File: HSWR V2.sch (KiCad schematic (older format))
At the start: 24 parts, among them P1 USB_B, P2 Interface, P3 IN+, P4 IN-, P5 MOTOR3, P6 MOTOR2, P7 MOTOR1

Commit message: - 100A in 50A geändert
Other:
- note added: "HSWR V2.0 200V 50A"
- note removed: "HSWR V2.0 200V 100A"
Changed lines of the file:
@@
 encoding utf-8
 Sheet 1 7
-Title "HSWR V2.0 200V 100A"
+Title "HSWR V2.0 200V 50A"
 Date "2017-02-05"
 Rev "2.0"
@@
 $EndComp
 Text Notes 800  1200 0    340  ~ 68
-HSWR V2.0 200V 100A
+HSWR V2.0 200V 50A
 $Bitmap
 Pos 10350 3100
@@
 C8 C8 08 D2 A9 87 39 1B F9 3D 64 10 3C A5 22 3B 19 76 2F 98 2B 2B 2B 1E 8F A7 AB AB 0B FB AC 1D
 B9 73 C8 EF 2C EC 8D 33 57 03 96 70 05 29 43 0C 6A C5 A8 D7 30 9E 87 2D DE BE E8 EA 73 2F 9C 18
-F1 B3 C3 9F 6D FA 1E FF 03 71 17 46 7E 55 DF FF 4E 00 00 00 00 49 45 4E 44 AE 42 60 82 0E
+F1 B3 C3 9F 6D FA 1E FF 03 71 17 46 7E 55 DF FF 4E 00 00 00 00 49 45 4E 44 AE 42 60 82 AB
 EndData
 $EndBitmap
@@
 20 08 82 20 08 12 3C 28 79 08 82 20 08 82 20 2D 08 4A 1E 82 20 08 82 20 48 0B 82 92 87 20 08 82
 20 08 D2 82 A0 E4 21 08 82 20 08 82 B4 20 28 79 08 82 20 08 82 20 2D 08 4A 1E 82 20 08 82 20 48
-0B F2 FF 19 12 7F 86 40 CA 02 9D 00 00 00 00 49 45 4E 44 AE 42 60 82 F3
+0B F2 FF 19 12 7F 86 40 CA 02 9D 00 00 00 00 49 45 4E 44 AE 42 60 82 FF
 EndData
 $EndBitmap
@@
 20 08 82 84 0E 7A 08 41 10 04 29 27 E8 21 04 41 10 A4 9C A0 87 10 04 41 90 72 82 1E 42 10 04 41
 CA 09 7A 08 41 10 04 29 27 E8 21 04 41 10 A4 9C FC 1F 60 28 4A EE 61 E4 B4 21 00 00 00 00 49 45
-4E 44 AE 42 60 82 00
+4E 44 AE 42 60 82 7F
 EndData
 $EndBitmap

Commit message: ~ removed/optionalised INA240 input filter ~ raised load resisitance of sense resistors for lower power loss ~ adopted old division factor on phase voltage sense deviders
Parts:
- R7: value 64k9 -> 160k
- R8: value 1k -> 3k3
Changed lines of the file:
@@
 C8 C8 08 D2 A9 87 39 1B F9 3D 64 10 3C A5 22 3B 19 76 2F 98 2B 2B 2B 1E 8F A7 AB AB 0B FB AC 1D
 B9 73 C8 EF 2C EC 8D 33 57 03 96 70 05 29 43 0C 6A C5 A8 D7 30 9E 87 2D DE BE E8 EA 73 2F 9C 18
-F1 B3 C3 9F 6D FA 1E FF 03 71 17 46 7E 55 DF FF 4E 00 00 00 00 49 45 4E 44 AE 42 60 82 AB
+F1 B3 C3 9F 6D FA 1E FF 03 71 17 46 7E 55 DF FF 4E 00 00 00 00 49 45 4E 44 AE 42 60 82 F5
 EndData
 $EndBitmap
@@
 20 08 82 20 08 12 3C 28 79 08 82 20 08 82 20 2D 08 4A 1E 82 20 08 82 20 48 0B 82 92 87 20 08 82
 20 08 D2 82 A0 E4 21 08 82 20 08 82 B4 20 28 79 08 82 20 08 82 20 2D 08 4A 1E 82 20 08 82 20 48
-0B F2 FF 19 12 7F 86 40 CA 02 9D 00 00 00 00 49 45 4E 44 AE 42 60 82 FF
+0B F2 FF 19 12 7F 86 40 CA 02 9D 00 00 00 00 49 45 4E 44 AE 42 60 82 00
 EndData
 $EndBitmap
@@
 P 5200 4350
 F 0 "R7" V 5280 4350 50  0000 C CNN
-F 1 "64k9" V 5200 4350 50  0000 C CNN
+F 1 "160k" V 5200 4350 50  0000 C CNN
 F 2 "Resistors_SMD:R_0805" V 5130 4350 30  0001 C CNN
 F 3 "" H 5200 4350 30  0000 C CNN
@@
 P 5200 4650
 F 0 "R8" V 5280 4650 50  0000 C CNN
-F 1 "1k" V 5200 4650 50  0000 C CNN
+F 1 "3k3" V 5200 4650 50  0000 C CNN
 F 2 "Resistors_SMD:R_0805" V 5130 4650 30  0001 C CNN
 F 3 "" H 5200 4650 30  0000 C CNN

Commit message: - changed dividers to 220k vs 3k3 - changed hall supply to +5V instead of +3V3
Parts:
- P1: symbol USB_B -> USB_B-RESCUE-HSWR_V2
- R7: value 160k -> 220k
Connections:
- wire segments 79 -> 77
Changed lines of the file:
@@
 C8 C8 08 D2 A9 87 39 1B F9 3D 64 10 3C A5 22 3B 19 76 2F 98 2B 2B 2B 1E 8F A7 AB AB 0B FB AC 1D
 B9 73 C8 EF 2C EC 8D 33 57 03 96 70 05 29 43 0C 6A C5 A8 D7 30 9E 87 2D DE BE E8 EA 73 2F 9C 18
-F1 B3 C3 9F 6D FA 1E FF 03 71 17 46 7E 55 DF FF 4E 00 00 00 00 49 45 4E 44 AE 42 60 82 F5
+F1 B3 C3 9F 6D FA 1E FF 03 71 17 46 7E 55 DF FF 4E 00 00 00 00 49 45 4E 44 AE 42 60 82
 EndData
 $EndBitmap
@@
 20 08 82 20 08 12 3C 28 79 08 82 20 08 82 20 2D 08 4A 1E 82 20 08 82 20 48 0B 82 92 87 20 08 82
 20 08 D2 82 A0 E4 21 08 82 20 08 82 B4 20 28 79 08 82 20 08 82 20 2D 08 4A 1E 82 20 08 82 20 48
-0B F2 FF 19 12 7F 86 40 CA 02 9D 00 00 00 00 49 45 4E 44 AE 42 60 82 00
+0B F2 FF 19 12 7F 86 40 CA 02 9D 00 00 00 00 49 45 4E 44 AE 42 60 82
 EndData
 $EndBitmap
@@
 P 5200 4350
 F 0 "R7" V 5280 4350 50  0000 C CNN
-F 1 "160k" V 5200 4350 50  0000 C CNN
+F 1 "220k" V 5200 4350 50  0000 C CNN
 F 2 "Resistors_SMD:R_0805" V 5130 4350 30  0001 C CNN
 F 3 "" H 5200 4350 30  0000 C CNN
@@
 20 08 82 84 0E 7A 08 41 10 04 29 27 E8 21 04 41 10 A4 9C A0 87 10 04 41 90 72 82 1E 42 10 04 41
 CA 09 7A 08 41 10 04 29 27 E8 21 04 41 10 A4 9C FC 1F 60 28 4A EE 61 E4 B4 21 00 00 00 00 49 45
-4E 44 AE 42 60 82 7F
+4E 44 AE 42 60 82
 EndData
 $EndBitmap
 $Comp
-L +3V3 #PWR013
-U 1 1 5899E248
-P 1300 4300
-F 0 "#PWR013" H 1300 4150 50  0001 C CNN
-F 1 "+3V3" V 1300 4550 50  0000 C CNN
-F 2 "" H 1300 4300 60  0000 C CNN
-F 3 "" H 1300 4300 60  0000 C CNN
-	1    1300 4300
-	0    1    1    0
-$EndComp
-$Comp
 L GND-RESCUE-BLDC_4 #PWR014
 U 1 1 5899E249
@@
 $EndComp
 $Comp
-L USB_B P1
+L USB_B-RESCUE-HSWR_V2 P1
 U 1 1 5899E24E
 P 950 3050
@@
 L +12VA #PWR022
 U 1 1 5899E265
-P 1350 3650
-F 0 "#PWR022" H 1350 3500 50  0001 C CNN
-F 1 "+12VA" H 1350 3790 50  0000 C CNN
-F 2 "" H 1350 3650 60  0000 C CNN
-F 3 "" H 1350 3650 60  0000 C CNN
-	1    1350 3650
-	1    0    0    -1
+P 1300 3700
+F 0 "#PWR022" H 1300 3550 50  0001 C CNN
+F 1 "+12VA" V 1300 3950 50  0000 C CNN
+F 2 "" H 1300 3700 60  0000 C CNN
+F 3 "" H 1300 3700 60  0000 C CNN
+	1    1300 3700
+	0    1    1    0
 $EndComp
-Wire Wire Line
-	1350 3650 1350 3700
-Wire Wire Line
-	1350 3700 1300 3700
 NoConn ~ 2550 4000
 $Comp
@@
 Wire Wire Line
 	1700 4400 1300 4400
-$Comp
-L CONN_01X18_20 P2
-U 1 1 5899E267
-P 1100 4650
-F 0 "P2" H 1100 5700 50  0000 C CNN
-F 1 "Interface" V 1200 4650 50  0000 C CNN
-F 2 "alexmod:XG4A_20_wo_56" H 1100 4650 60  0001 C CNN
-F 3 "" H 1100 4650 60  0000 C CNN
-	1    1100 4650
-	-1   0    0    -1
-$EndComp
 Wire Wire Line
 	7650 3800 8300 3800
@@
 Wire Wire Line
 	5950 3600 5950 6300
+$Comp
+L +5V #PWR?
+U 1 1 5B67A97B
+P 1300 4300
+F 0 "#PWR?" H 1300 4150 50  0001 C CNN
+F 1 "+5V" V 1300 4550 50  0000 C CNN
+F 2 "" H 1300 4300 60  0000 C CNN
+F 3 "" H 1300 4300 60  0000 C CNN
+	1    1300 4300
+	0    1    1    0
+$EndComp
+$Comp
+L CONN_01X18_20 P2
+U 1 1 5899E267
+P 1100 4650
+F 0 "P2" H 1100 5700 50  0000 C CNN
+F 1 "Interface" V 1200 4650 50  0000 C CNN
+F 2 "alexmod:XG4A_20_wo_56" H 1100 4650 60  0001 C CNN
+F 3 "" H 1100 4650 60  0000 C CNN
+	1    1100 4650
+	-1   0    0    -1
+$EndComp
 $EndSCHEMATC

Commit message: - updated project to 5.0.0 - added ignore file
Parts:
- C1: symbol C-RESCUE-BLDC_4 -> HSWR-V2-rescue:C-RESCUE-BLDC_4
- C2: symbol C -> Device:C
- D1: symbol D_Schottky_Small -> Device:D_Schottky_Small
- D2, D3, D4: symbol LED-RESCUE-BLDC_4 -> HSWR-V2-rescue:LED-RESCUE-BLDC_4
- P1: symbol USB_B-RESCUE-HSWR_V2 -> HSWR-V2-rescue:USB_B-RESCUE-HSWR_V2
- P2: symbol CONN_01X18_20 -> HSWR-V2-rescue:CONN_01X18_20
- P3, P4, P5, P6, P7: symbol CONN_1 -> HSWR-V2-rescue:CONN_1
- R1, R11, R2, R7, R8: symbol R -> Device:R
- R10, R3, R4, R5, R6, R9: symbol R-RESCUE-BLDC_4 -> HSWR-V2-rescue:R-RESCUE-BLDC_4
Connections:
- wire segments 77 -> 76
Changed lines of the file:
@@
-EESchema Schematic File Version 2
-LIBS:HSWR V2-rescue
-LIBS:power
-LIBS:device
-LIBS:transistors
-LIBS:conn
-LIBS:linear
-LIBS:regul
-LIBS:74xx
-LIBS:cmos4000
-LIBS:adc-dac
-LIBS:memory
-LIBS:xilinx
-LIBS:microcontrollers
-LIBS:dsp
-LIBS:microchip
-LIBS:analog_switches
-LIBS:motorola
-LIBS:texas
-LIBS:intel
-LIBS:audio
-LIBS:interface
-LIBS:digital-audio
-LIBS:philips
-LIBS:display
-LIBS:cypress
-LIBS:siliconi
-LIBS:opto
-LIBS:atmel
-LIBS:contrib
-LIBS:valves
+EESchema Schematic File Version 4
 LIBS:HSWR V2-cache
-EELAYER 25 0
+EELAYER 26 0
 EELAYER END
 $Descr A4 11693 8268
@@
 $EndSheet
 $Comp
-L GND-RESCUE-BLDC_4 #PWR01
+L HSWR-V2-rescue:GND-RESCUE-BLDC_4 #PWR01
 U 1 1 5895E67B
 P 8850 4900
@@
 $EndComp
 $Comp
-L CONN_1 P4
+L HSWR-V2-rescue:CONN_1 P4
 U 1 1 5895E67C
 P 8650 1050
@@
 $EndComp
 $Comp
-L CONN_1 P3
+L HSWR-V2-rescue:CONN_1 P3
 U 1 1 5895E67D
 P 8650 850
@@
 $EndComp
 $Comp
-L CONN_1 P5
+L HSWR-V2-rescue:CONN_1 P5
 U 1 1 5895E67E
 P 9850 2600
@@
 $EndComp
 $Comp
-L CONN_1 P6
+L HSWR-V2-rescue:CONN_1 P6
 U 1 1 5895E67F
 P 9850 2750
@@
 $EndComp
 $Comp
-L CONN_1 P7
+L HSWR-V2-rescue:CONN_1 P7
 U 1 1 5895E680
 P 9850 3550
@@
 $Bitmap
 Pos 10350 3100
-Scale 1,000000
+Scale 1.000000
 Data
 89 50 4E 47 0D 0A 1A 0A 00 00 00 0D 49 48 44 52 00 00 00 B9 00 00 00 C6 08 02 00 00 00 01 BB B6
@@
 $Bitmap
 Pos 5000 4400
-Scale 0,000000
+Scale 0.000000
 Data
 89 50 4E 47 0D 0A 1A 0A 00 00 00 0D 49 48 44 52 00 00 03 4C 00 00 02 2D 08 02 00 00 00 85 20 6D
@@
 Wire Wire Line
 	8800 1150 8800 1050
-Wire Wire Line
-	9700 2600 9700 2600
 Wire Notes Line
 	8350 650  9400 650
@@
 	7650 2300 8300 2300
 $Comp
-L GNDPWR #PWR02
+L HSWR-V2-rescue:GNDPWR #PWR02
 U 1 1 5895E699
 P 9150 4900
@@
 $EndComp
 $Comp
-L +BATT #PWR03
+L power:+BATT #PWR03
 U 1 1 5895E69C
 P 5200 4200
@@
 $EndComp
 $Comp
-L GND-RESCUE-BLDC_4 #PWR04
+L HSWR-V2-rescue:GND-RESCUE-BLDC_4 #PWR04
 U 1 1 5895E69D
 P 5200 4800
@@
 $EndComp
 $Comp
-L R R7
+L Device:R R7
 U 1 1 5895E69E
 P 5200 4350
@@
 $EndComp
 $Comp
-L R R8
+L Device:R R8
 U 1 1 5895E69F
 P 5200 4650
@@
 Connection ~ 5200 4500
 $Comp
-L +BATT #PWR05
+L power:+BATT #PWR05
 U 1 1 5895E6AB
 P 8800 850
@@
 $EndComp
 $Comp
-L R R11
+L Device:R R11
 U 1 1 5895E6AC
 P 9000 4800
@@
 $EndComp
 $Comp
-L GNDPWR #PWR06
+L HSWR-V2-rescue:GNDPWR #PWR06
 U 1 1 5895E6AD
 P 8800 1150
@@
 $EndComp
 $Comp
-L R-RESCUE-BLDC_4 R9
+L HSWR-V2-rescue:R-RESCUE-BLDC_4 R9
 U 1 1 58962D54
 P 6200 5950
@@
 $EndComp
 $Comp
-L R-RESCUE-BLDC_4 R10
+L HSWR-V2-rescue:R-RESCUE-BLDC_4 R10
 U 1 1 58962D5B
 P 6200 6650
@@
 $EndComp
 $Comp
-L GND-RESCUE-BLDC_4 #PWR07
+L HSWR-V2-rescue:GND-RESCUE-BLDC_4 #PWR07
 U 1 1 58962D62
 P 6200 7150
@@
 $EndComp
 Wire Wire Line
-	6200 6900 6200 7150
+	6200 6900 6200 7000
 Wire Wire Line
 	6450 6800 6450 7000
@@
 Connection ~ 6200 7000
 Wire Wire Line
-	6200 6200 6200 6400
+	6200 6200 6200 6300
 Wire Wire Line
-	5950 6300 6450 6300
+	5950 6300 6200 6300
 Wire Wire Line
 	6450 6300 6450 6500
@@
 	6200 5600 6200 5700
 $Comp
-L +3V3 #PWR08
+L power:+3V3 #PWR08
 U 1 1 58962D75
 P 6200 5600
@@
 $EndComp
 $Comp
-L C C2
+L Device:C C2
 U 1 1 58962D7B
 P 6450 6650
@@
 $EndComp
 $Comp
-L C-RESCUE-BLDC_4 C1
+L HSWR-V2-rescue:C-RESCUE-BLDC_4 C1
 U 1 1 5899E222
 P 2750 6050
@@
 $EndComp
 $Comp
-L R-RESCUE-BLDC_4 R3
+L HSWR-V2-rescue:R-RESCUE-BLDC_4 R3
 U 1 1 5899E223
 P 2400 5500
@@
 $EndComp
 $Comp
-L GND-RESCUE-BLDC_4 #PWR09
+L HSWR-V2-rescue:GND-RESCUE-BLDC_4 #PWR09
 U 1 1 5899E224
 P 2750 6250
@@
 $EndSheet
 $Comp
-L R-RESCUE-BLDC_4 R6
+L HSWR-V2-rescue:R-RESCUE-BLDC_4 R6
 U 1 1 5899E227
 P 4750 5950
@@
 $EndComp
 $Comp
-L LED-RESCUE-BLDC_4 D4
+L HSWR-V2-rescue:LED-RESCUE-BLDC_4 D4
 U 1 1 5899E228
 P 5200 5950
@@
 $EndComp
 $Comp
-L GND-RESCUE-BLDC_4 #PWR010
+L HSWR-V2-rescue:GND-RESCUE-BLDC_4 #PWR010
 U 1 1 5899E229
 P 5400 5950
@@
 $EndComp
 $Comp
-L R-RESCUE-BLDC_4 R5
+L HSWR-V2-rescue:R-RESCUE-BLDC_4 R5
 U 1 1 5899E22A
 P 4750 5650
@@
 $EndComp
 $Comp
-L LED-RESCUE-BLDC_4 D3
+L HSWR-V2-rescue:LED-RESCUE-BLDC_4 D3
 U 1 1 5899E22B
 P 5200 5650
@@
 $EndComp
 $Comp
-L GND-RESCUE-BLDC_4 #PWR011
+L HSWR-V2-rescue:GND-RESCUE-BLDC_4 #PWR011
 U 1 1 5899E22C
 P 5400 5650
@@
 $EndComp
 $Comp
-L LED-RESCUE-BLDC_4 D2
+L HSWR-V2-rescue:LED-RESCUE-BLDC_4 D2
 U 1 1 5899E22D
 P 5200 5350
@@
 $EndComp
 $Comp
-L R-RESCUE-BLDC_4 R4
+L HSWR-V2-rescue:R-RESCUE-BLDC_4 R4
 U 1 1 5899E22E
 P 4750 5350
@@
 $EndComp
 $Comp
-L GND-RESCUE-BLDC_4 #PWR012
+L HSWR-V2-rescue:GND-RESCUE-BLDC_4 #PWR012
 U 1 1 5899E22F
 P 5400 5350
@@
 $Bitmap
 Pos 5000 5100
-Scale 0,000000
+Scale 0.000000
 Data
 89 50 4E 47 0D 0A 1A 0A 00 00 00 0D 49 48 44 52 00 00 02 2D 00 00 03 4C 08 02 00 00 00 1F 54 0A
@@
 $EndBitmap
 $Comp
-L GND-RESCUE-BLDC_4 #PWR014
+L HSWR-V2-rescue:GND-RESCUE-BLDC_4 #PWR014
 U 1 1 5899E249
 P 1300 4800
@@
 $EndComp
 $Comp
-L GND-RESCUE-BLDC_4 #PWR015
+L HSWR-V2-rescue:GND-RESCUE-BLDC_4 #PWR015
 U 1 1 5899E24A
 P 1300 5400
@@
 $EndComp
 $Comp
-L +3V3 #PWR016
+L power:+3V3 #PWR016
 U 1 1 5899E24B
 P 1300 4900
@@
 $EndComp
 $Comp
-L GND-RESCUE-BLDC_4 #PWR017
+L HSWR-V2-rescue:GND-RESCUE-BLDC_4 #PWR017
 U 1 1 5899E24C
 P 1300 5600
@@
 $EndComp
 $Comp
-L +3V3 #PWR018
+L power:+3V3 #PWR018
 U 1 1 5899E24D
 P 4500 5350
@@
 $EndComp
 $Comp
-L USB_B-RESCUE-HSWR_V2 P1
+L HSWR-V2-rescue:USB_B-RESCUE-HSWR_V2 P1
 U 1 1 5899E24E
 P 950 3050
@@
 $EndComp
 $Comp
-L GND-RESCUE-BLDC_4 #PWR019
+L HSWR-V2-rescue:GND-RESCUE-BLDC_4 #PWR019
 U 1 1 5899E24F
 P 1250 3150
@@
 $EndComp
 $Comp
-L GND-RESCUE-BLDC_4 #PWR020
+L HSWR-V2-rescue:GND-RESCUE-BLDC_4 #PWR020
 U 1 1 5899E250
 P 850 3350
@@
 	1700 3050 2950 3050
 Wire Wire Line
-	5000 5950 5000 5950
-Wire Wire Line
-	5400 5950 5400 5950
-Wire Wire Line
-	5000 5650 5000 5650
-Wire Wire Line
-	5400 5650 5400 5650
-Wire Wire Line
 	1700 3900 1300 3900
 Wire Wire Line
@@
 	2750 5850 2750 5500
 Wire Wire Line
-	2650 5500 2950 5500
+	2650 5500 2750 5500
 Connection ~ 2750 5500
 $Sheet
@@
 $EndSheet
 $Comp
-L D_Schottky_Small D1
+L Device:D_Schottky_Small D1
 U 1 1 5899E260
 P 1300 2700
@@
 $EndComp
 $Comp
-L +5V #PWR021
+L power:+5V #PWR021
 U 1 1 5899E261
 P 1300 2600
@@
 $EndComp
 $Comp
-L R R1
+L Device:R R1
 U 1 1 5899E262
 P 1550 2950
@@
 $EndComp
 $Comp
-L R R2
+L Device:R R2
 U 1 1 5899E263
 P 1550 3050
@@
 	1300 2850 1250 2850
 $Comp
-L +12VA #PWR022
+L power:+12VA #PWR022
 U 1 1 5899E265
 P 1300 3700
@@
 NoConn ~ 2550 4000
 $Comp
-L Earth #PWR023
+L power:Earth #PWR023
 U 1 1 5899E266
 P 1300 4000
@@
 	5950 3600 5950 6300
 $Comp
-L +5V #PWR?
+L power:+5V #PWR0101
 U 1 1 5B67A97B
 P 1300 4300
-F 0 "#PWR?" H 1300 4150 50  0001 C CNN
+F 0 "#PWR0101" H 1300 4150 50  0001 C CNN
 F 1 "+5V" V 1300 4550 50  0000 C CNN
 F 2 "" H 1300 4300 60  0000 C CNN
@@
 $EndComp
 $Comp
-L CONN_01X18_20 P2
+L HSWR-V2-rescue:CONN_01X18_20 P2
 U 1 1 5899E267
 P 1100 4650
@@
 	-1   0    0    -1
 $EndComp
+Wire Wire Line
+	6200 7000 6200 7150
+Wire Wire Line
+	6200 6300 6200 6400
+Wire Wire Line
+	6200 6300 6450 6300
+Wire Wire Line
+	2750 5500 2950 5500
 $EndSCHEMATC

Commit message: - updated to VESC6 architecture - still some things to do in schematic
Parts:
- removed C1: 100n, Capacitors_SMD:C_0805, symbol HSWR-V2-rescue:C-RESCUE-BLDC_4
- removed D1: SS14, Diodes_SMD:SMA_Standard, symbol Device:D_Schottky_Small
- removed D2: LED, LEDs:LED_0805, symbol HSWR-V2-rescue:LED-RESCUE-BLDC_4
- removed D3: GREEN, LEDs:LED_0805, symbol HSWR-V2-rescue:LED-RESCUE-BLDC_4
- removed D4: RED, LEDs:LED_0805, symbol HSWR-V2-rescue:LED-RESCUE-BLDC_4
- removed P1: USB_B, alexmod:USBB_vert, symbol HSWR-V2-rescue:USB_B-RESCUE-HSWR_V2
- removed P2: Interface, alexmod:XG4A_20_wo_56, symbol HSWR-V2-rescue:CONN_01X18_20
- removed P3: IN+, Mounting_Holes:MountingHole_6.5mm_Pad_Via, symbol HSWR-V2-rescue:CONN_1
- removed P4: IN-, Mounting_Holes:MountingHole_6.5mm_Pad_Via, symbol HSWR-V2-rescue:CONN_1
- removed P5: MOTOR3, Mounting_Holes:MountingHole_6.5mm_Pad_Via, symbol HSWR-V2-rescue:CONN_1
- removed P6: MOTOR2, Mounting_Holes:MountingHole_6.5mm_Pad_Via, symbol HSWR-V2-rescue:CONN_1
- removed P7: MOTOR1, Mounting_Holes:MountingHole_6.5mm_Pad_Via, symbol HSWR-V2-rescue:CONN_1
- removed R10: 10k, Resistors_SMD:R_0805, symbol HSWR-V2-rescue:R-RESCUE-BLDC_4
- removed R3, R4: 2k2, Resistors_SMD:R_0805, symbol HSWR-V2-rescue:R-RESCUE-BLDC_4
- removed R5, R6: 120R, Resistors_SMD:R_0805, symbol HSWR-V2-rescue:R-RESCUE-BLDC_4
- removed R9: NTC 10k, Resistors_SMD:R_0603, symbol HSWR-V2-rescue:R-RESCUE-BLDC_4
- added D1, D2, D3: LED, LED_SMD:LED_0805_2012Metric, symbol Device:LED
- added J1: CAN, symbol Connector:Conn_01x04_Male
- added J2: Motor, symbol Connector:Conn_01x06_Male
- added J3: IO, symbol Connector:Conn_01x08_Male
- added J4: USB_B, Connector_USB:USB_B_TE_5787834_Vertical, symbol Connector:USB_B
- added J5: B+, MountingHole:MountingHole_6.5mm_Pad_Via, symbol Connector:Conn_01x01_Male
- added J6: B-, MountingHole:MountingHole_6.5mm_Pad_Via, symbol Connector:Conn_01x01_Male
- added J7: U, MountingHole:MountingHole_6.5mm_Pad_Via, symbol Connector:Conn_01x01_Male
- added J8: V, MountingHole:MountingHole_6.5mm_Pad_Via, symbol Connector:Conn_01x01_Male
- added J9: W, MountingHole:MountingHole_6.5mm_Pad_Via, symbol Connector:Conn_01x01_Male
- added JP1: 5V/3V3, Jumper:SolderJumper-3_P1.3mm_Open_RoundedPad1.0x1.5mm, symbol Jumper:SolderJumper_3_Open
- added JP2, JP3: opt., Jumper:SolderJumper-2_P1.3mm_Open_RoundedPad1.0x1.5mm, symbol Jumper:SolderJumper_2_Open
- added R10: NTC, Resistor_SMD:R_0603_1608Metric, symbol Device:R
- added R3, R4: 1k5, Resistor_SMD:R_0805_2012Metric, symbol Device:R
- added R5: 470R, Resistor_SMD:R_0805_2012Metric, symbol Device:R
- added R6, R9: 120R, Resistor_SMD:R_0805_2012Metric, symbol Device:R
- C2: footprint Capacitors_SMD:C_0805 -> Capacitor_SMD:C_0805_2012Metric
- R1, R2: value 22R -> 1k; footprint Resistors_SMD:R_0805 -> Resistor_SMD:R_0805_2012Metric
- R11: value R -> 10k; footprint Resistors_SMD:R_0805 -> Resistor_SMD:R_0805_2012Metric
- R7: value 220k -> 300k; footprint Resistors_SMD:R_0805 -> Resistor_SMD:R_0805_2012Metric
- R8: value 3k3 -> 4k7; footprint Resistors_SMD:R_0805 -> Resistor_SMD:R_0805_2012Metric
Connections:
- wire segments 76 -> 74
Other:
- note added: "HSWR V3.0 200V 100A"
- note removed: "100R if used as\nservo output"
- note removed: "Connect signal ground and\npower ground in one place only"
- note removed: "HSWR V2.0 200V 50A"
- moved on the sheet: C2

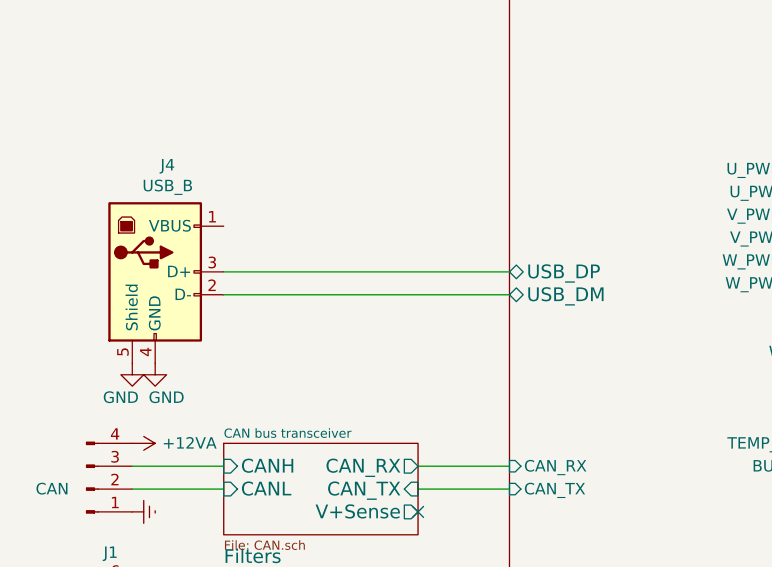
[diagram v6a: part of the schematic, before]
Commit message: - gate drivers routed - CSAs routed - HV/PA nets routed
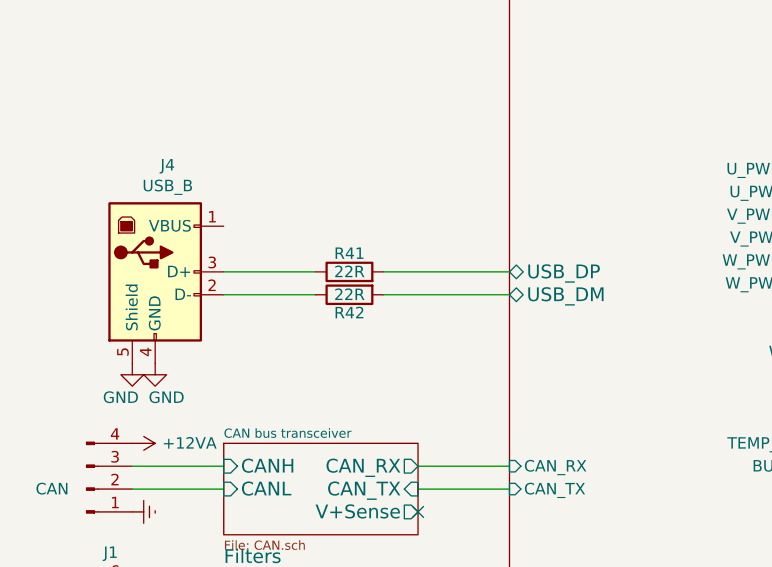
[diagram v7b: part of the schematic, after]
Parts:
- added R41, R42: 22R, Resistor_SMD:R_0805_2012Metric, symbol Device:R
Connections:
- net MCU/USB_DM: now also R42.2; no longer J4.2 (D-)
- net MCU/USB_DP: now also R41.2; no longer J4.3 (D+)
- new net: J4.3 (D+), R41.1
- new net: J4.2 (D-), R42.1
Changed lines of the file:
@@
 	2950 3900 2550 3900
-Wire Wire Line
-	1700 2950 2950 2950
-Wire Wire Line
-	1700 3050 2950 3050
 Wire Wire Line
 	1700 3900 1300 3900
@@
 Wire Wire Line
 	1300 5750 2950 5750
+$Comp
+L Device:R R41
+U 1 1 5C9C4B7D
+P 2250 2950
+F 0 "R41" V 2330 2950 50  0000 C CNN
+F 1 "22R" V 2250 2950 50  0000 C CNN
+F 2 "Resistor_SMD:R_0805_2012Metric" V 2180 2950 30  0001 C CNN
+F 3 "" H 2250 2950 30  0000 C CNN
+	1    2250 2950
+	0    -1   -1   0
+$EndComp
+Wire Wire Line
+	2100 2950 1700 2950
+Wire Wire Line
+	2400 2950 2950 2950
+$Comp
+L Device:R R42
+U 1 1 5C9D445C
+P 2250 3050
+F 0 "R42" V 2330 3050 50  0000 C CNN
+F 1 "22R" V 2250 3050 50  0000 C CNN
+F 2 "Resistor_SMD:R_0805_2012Metric" V 2180 3050 30  0001 C CNN
+F 3 "" H 2250 3050 30  0000 C CNN
+	1    2250 3050
+	0    -1   1    0
+$EndComp
+Wire Wire Line
+	2100 3050 1700 3050
+Wire Wire Line
+	2400 3050 2950 3050
 $EndSCHEMATC
